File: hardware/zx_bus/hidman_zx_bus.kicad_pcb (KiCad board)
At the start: 2 copper layers, 99.1 x 55 mm, 55 parts, among them J1 X1A, J10 JOY_ENABLE, J11 TAPE IN, J12 USB EXT, J13 PS/2 Mouse External Bracket, J14 PS/2 Keyboard External Bracket, J2 X1B, J3 UART, J4 USB_A, J5 USB_A, J7 Mouse / Key, J8 GOTEK, J9 JTAG, Q1 BSS123, Q2 BSS123, Q3 BSS123, SW1 RESET, SW2 BOOT0, U1 CH559L, U2 EPM3128ATC100, U3 AMS1117-3.3, U4 74LVC1G125DB, U6 IP4220CZ6, Y1 12MHz

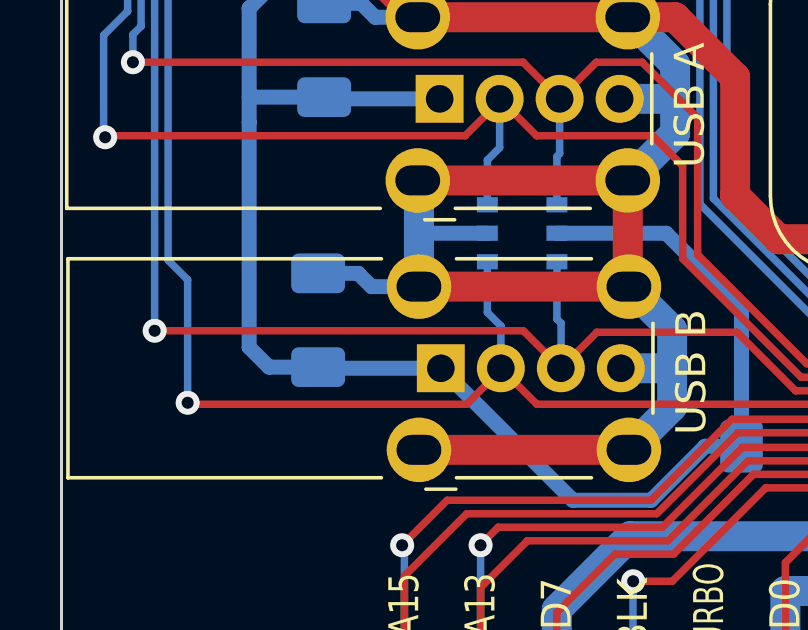
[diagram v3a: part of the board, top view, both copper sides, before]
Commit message: Fixed IP4220CZ6 ESD protection IC DM_B/DP_B connections.
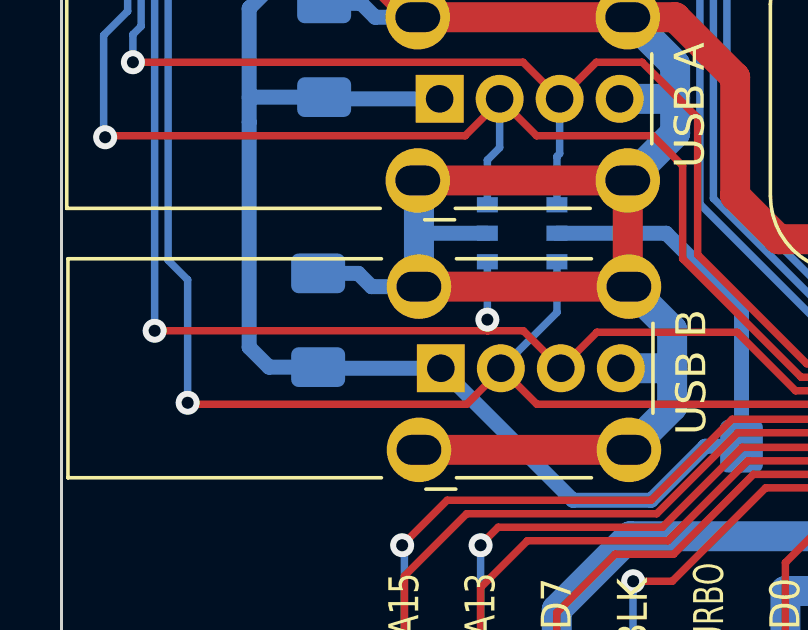
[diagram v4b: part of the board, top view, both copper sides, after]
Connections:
- U6 pad 1: /DM_B -> /DP_B
- U6 pad 6: /DP_B -> /DM_B
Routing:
- net /DP_B: track 90.7 -> 89.4 mm, vias 1 -> 2
- net /DM_B: track 93.9 -> 94.5 mm
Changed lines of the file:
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@@
 			(size 0.7 0.51)
 			(layers "B.Cu" "B.Paste" "B.Mask")
-			(net 83 "/DM_B")
+			(net 82 "/DP_B")
 			(pinfunction "D+")
 			(pintype "bidirectional")
@@
 			(size 0.7 0.51)
 			(layers "B.Cu" "B.Paste" "B.Mask")
-			(net 82 "/DP_B")
+			(net 83 "/DM_B")
 			(pinfunction "D-")
 			(pintype "bidirectional")
@@
 	)
 	(segment
+		(start 56.75 129.65)
+		(end 57.94 129.65)
+		(width 0.25)
+		(layer "F.Cu")
+		(net 82)
+	)
+	(segment
 		(start 57.94 129.65)
 		(end 59.19 130.9)
@@
 	)
 	(segment
-		(start 65.063604 129.7)
-		(end 60.39 129.7)
+		(start 56.75 129.29)
+		(end 56.75 129.65)
 		(width 0.25)
 		(layer "F.Cu")
@@
 	)
 	(segment
-		(start 60.39 129.7)
-		(end 59.19 130.9)
+		(start 65.063604 129.7)
+		(end 60.39 129.7)
 		(width 0.25)
 		(layer "F.Cu")
@@
 	)
 	(segment
-		(start 45.65 129.65)
-		(end 57.94 129.65)
+		(start 60.39 129.7)
+		(end 59.19 130.9)
 		(width 0.25)
 		(layer "F.Cu")
@@
 	)
 	(segment
+		(start 45.65 129.65)
+		(end 56.75 129.65)
+		(width 0.25)
+		(layer "F.Cu")
+		(net 82)
+	)
+	(segment
+		(start 56.74 129.28)
+		(end 56.75 129.29)
+		(width 0.25)
+		(layer "F.Cu")
+		(net 82)
+	)
+	(segment
 		(start 82.0125 127.5125)
 		(end 82.0125 129.251104)
@@
 	)
 	(via
+		(at 56.74 129.28)
+		(size 0.8)
+		(drill 0.4)
+		(layers "F.Cu" "B.Cu")
+		(net 82)
+	)
+	(via
 		(at 45.65 129.65)
 		(size 0.8)
@@
 	)
 	(segment
-		(start 59.06 127.35)
-		(end 59.06 129.26)
-		(width 0.25)
-		(layer "B.Cu")
-		(net 82)
-	)
-	(segment
 		(start 47.9 104.75)
 		(end 48.963604 104.75)
@@
 	)
 	(segment
-		(start 59.06 129.26)
-		(end 59.2 129.4)
-		(width 0.25)
-		(layer "B.Cu")
-		(net 82)
-	)
-	(segment
 		(start 48.963604 104.75)
 		(end 51.963604 101.75)
@@
 	)
 	(segment
-		(start 59.2 129.4)
-		(end 59.2 130.89)
+		(start 51.963604 101.75)
+		(end 65.25 101.75)
 		(width 0.25)
 		(layer "B.Cu")
@@
 	)
 	(segment
-		(start 51.963604 101.75)
-		(end 65.25 101.75)
+		(start 56.74 129.28)
+		(end 56.74 127.35)
 		(width 0.25)
 		(layer "B.Cu")
@@
 	)
 	(segment
+		(start 57.19 130.9)
+		(end 57.2 130.9)
+		(width 0.25)
+		(layer "B.Cu")
+		(net 83)
+	)
+	(segment
 		(start 46.75 127.95)
 		(end 46.1 127.3)
@@
 	)
 	(segment
+		(start 59.06 129.04)
+		(end 59.06 127.35)
+		(width 0.25)
+		(layer "B.Cu")
+		(net 83)
+	)
+	(segment
 		(start 50.75 103.6)
 		(end 56.463173 103.6)
@@
 	)
 	(segment
-		(start 57.19 130.9)
-		(end 57.19 129.49)
+		(start 57.2 130.9)
+		(end 59.06 129.04)
 		(width 0.25)
 		(layer "B.Cu")
@@
 		(width 0.25)
 		(layer "B.Cu")
-		(net 83)
-	)
-	(segment
-		(start 56.74 129.04)
-		(end 56.74 127.35)
-		(width 0.25)
-		(layer "B.Cu")
-		(net 83)
-	)
-	(segment
-		(start 57.19 129.49)
-		(end 56.74 129.04)
-		(width 0.25)
-		(layer "B.Cu")

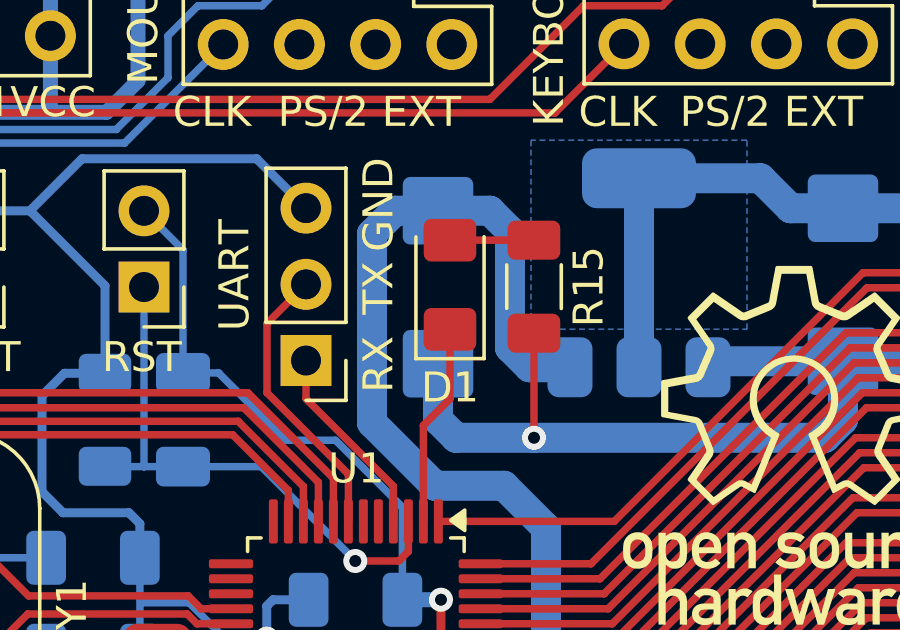
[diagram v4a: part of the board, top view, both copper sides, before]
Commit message: Correct LED polarity on ZX BUS PCB.
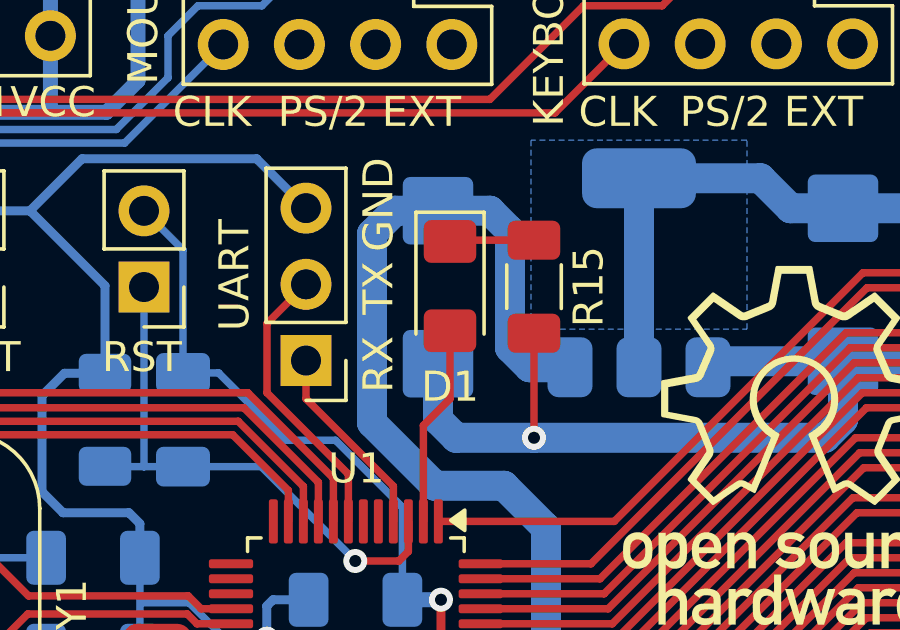
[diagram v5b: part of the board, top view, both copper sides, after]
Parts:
- turned D1 to -90 degrees
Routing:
- net Net-(D1-K): track 0.00 -> 2.80 mm
- net /P1_7: track 9.57 -> 6.77 mm
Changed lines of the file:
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@@
 	(footprint "LED_SMD:LED_1206_3216Metric_Pad1.42x1.75mm_HandSolder"
 		(layer "F.Cu")
-		(at 84.9 111.3 90)
+		(at 84.9 111.345 -90)
 		(descr "LED SMD 1206 (3216 Metric), square (rectangular) end terminal, IPC_7351 nominal, (Body size source: http://www.tortai-tech.com/upload/download/2011102023233369053.pdf), generated with kicad-footprint-generator")
 		(tags "LED handsolder")
 		(property "Reference" "D1"
-			(at -3.424999 0.000001 180)
+			(at 3.355 0.000001 180)
 			(layer "F.SilkS")
 			(effects
@@
 		)
 		(property "Value" "LED"
-			(at 0 1.82 -90)
+			(at 0 1.82 90)
 			(layer "F.Fab")
 			(effects
@@
 		)
 		(property "Footprint" "LED_SMD:LED_1206_3216Metric_Pad1.42x1.75mm_HandSolder"
-			(at 0 0 90)
+			(at 0 0 -90)
 			(unlocked yes)
 			(layer "F.Fab")
@@
 		)
 		(property "Datasheet" ""
-			(at 0 0 90)
+			(at 0 0 -90)
 			(unlocked yes)
 			(layer "F.Fab")
@@
 		)
 		(property "Description" "Light emitting diode"
-			(at 0 0 90)
+			(at 0 0 -90)
 			(unlocked yes)
 			(layer "F.Fab")
@@
 		(attr smd)
 		(fp_line
-			(start 1.6 -1.135)
-			(end -2.46 -1.135)
+			(start -2.46 1.135)
+			(end 1.6 1.135)
 			(stroke
 				(width 0.12)
@@
 		)
 		(fp_line
-			(start -2.46 1.135)
-			(end 1.6 1.135)
+			(start 1.6 -1.135)
+			(end -2.46 -1.135)
 			(stroke
 				(width 0.12)
@@
 		)
 		(fp_line
-			(start 2.45 -1.12)
-			(end 2.45 1.12)
+			(start -2.45 1.12)
+			(end -2.45 -1.12)
 			(stroke
 				(width 0.05)
@@
 		)
 		(fp_line
-			(start -2.45 -1.12)
-			(end 2.45 -1.12)
+			(start 2.45 1.12)
+			(end -2.45 1.12)
 			(stroke
 				(width 0.05)
@@
 		)
 		(fp_line
-			(start 2.45 1.12)
-			(end -2.45 1.12)
+			(start -2.45 -1.12)
+			(end 2.45 -1.12)
 			(stroke
 				(width 0.05)
@@
 		)
 		(fp_line
-			(start -2.45 1.12)
-			(end -2.45 -1.12)
+			(start 2.45 -1.12)
+			(end 2.45 1.12)
 			(stroke
 				(width 0.05)
@@
 		)
 		(fp_line
-			(start 1.6 -0.8)
-			(end -1.2 -0.8)
+			(start -1.6 0.8)
+			(end 1.6 0.8)
 			(stroke
 				(width 0.1)
@@
 		)
 		(fp_line
-			(start -1.2 -0.8)
-			(end -1.6 -0.4)
+			(start 1.6 0.8)
+			(end 1.6 -0.8)
 			(stroke
 				(width 0.1)
@@
 		)
 		(fp_line
-			(start 1.6 0.8)
-			(end 1.6 -0.8)
+			(start -1.2 -0.8)
+			(end -1.6 -0.4)
 			(stroke
 				(width 0.1)
@@
 		)
 		(fp_line
-			(start -1.6 0.8)
-			(end 1.6 0.8)
+			(start 1.6 -0.8)
+			(end -1.2 -0.8)
 			(stroke
 				(width 0.1)
@@
 		)
 		(fp_text user "${REFERENCE}"
-			(at 0 0 -90)
+			(at 0 0 90)
 			(layer "F.Fab")
 			(effects
@@
 		)
 		(pad "1" smd roundrect
-			(at -1.4875 0 90)
+			(at -1.4875 0 270)
 			(size 1.425 1.75)
 			(layers "F.Cu" "F.Paste" "F.Mask")
@@
 		)
 		(pad "2" smd roundrect
-			(at 1.4875 0 90)
+			(at 1.4875 0 270)
 			(size 1.425 1.75)
 			(layers "F.Cu" "F.Paste" "F.Mask")
@@
 	)
 	(segment
-		(start 84.9 115.1)
-		(end 84.9 112.7875)
-		(width 0.25)
-		(layer "F.Cu")
-		(net 79)
-	)
-	(segment
 		(start 84.9 109.8125)
 		(end 87.69875 109.8125)
 		(width 0.25)
 		(layer "F.Cu")
-		(net 79)
+		(net 78)
 	)
 	(segment
@@
 		(width 0.25)
 		(layer "F.Cu")
+		(net 78)
+	)
+	(segment
+		(start 84.9 115.1)
+		(end 84.9 112.7875)
+		(width 0.25)
+		(layer "F.Cu")

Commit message: Update ZX BUS PCB version to 1.1.
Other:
- board text added: "V.1.1"
- board text removed: "V.1.0"
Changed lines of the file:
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@@
 		)
 	)
-	(gr_text "V.1.0"
+	(gr_text "V.1.1"
 		(at 48.925 137.9 0)
 		(layer "B.SilkS")
